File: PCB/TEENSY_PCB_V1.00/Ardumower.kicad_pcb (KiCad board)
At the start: 2 copper layers, 169.8 x 97 mm, 48 parts, among them J10 Sonar_R, J12 Sonar_L, J13 P_Right, J14 Buzzer, J15 Button, J19 P_Left, J2 I2C2, J21 PCB_2, J23 Ser1, J25 5V IN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

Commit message: gy521 test
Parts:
- added JP1: Jumper_3.3V, Connector_PinSocket_2.54mm:PinSocket_1x03_P2.54mm_Vertical, F.Cu at (256.7, 60.1)
- added U2: MAX5215, teensy_library-master:GY-521, F.Cu at (77.9, 29.0)
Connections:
- D8 pad 1: +3V3 -> Net-(D8-Pad1)
- U3 pad 46: (no net) -> Net-(JP1-Pad3)

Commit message: test
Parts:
- removed J21: PCB_2, Connector_JST:JST_XH_B6B-XH-A_1x06_P2.50mm_Vertical
- removed J23: Ser1, Connector_JST:JST_XH_B5B-XH-A_1x05_P2.50mm_Vertical
- removed J38: ODO_Left, Connector_JST:JST_XH_B4B-XH-A_1x04_P2.50mm_Vertical
- removed J39: ODO_Right, Connector_JST:JST_XH_B4B-XH-A_1x04_P2.50mm_Vertical
- removed J40: Motor_Right1, Connector_JST:JST_XH_B5B-XH-A_1x05_P2.50mm_Vertical
- removed J41: Motor_Left1, Connector_JST:JST_XH_B5B-XH-A_1x05_P2.50mm_Vertical
- removed J42: Cutter, Connector_JST:JST_XH_B5B-XH-A_1x05_P2.50mm_Vertical
- removed R14: 1KO, Resistor_THT:R_Axial_DIN0207_L6.3mm_D2.5mm_P2.54mm_Vertical
- removed R16, R17: 1,5KO, Resistor_THT:R_Axial_DIN0207_L6.3mm_D2.5mm_P2.54mm_Vertical
- added J1: ODO_Left, Connector_JST:JST_XH_B4B-XH-A_1x04_P2.50mm_Vertical, F.Cu at (168.5, 111.0)
- added J11: Cutter, Connector_JST:JST_XH_B5B-XH-A_1x05_P2.50mm_Vertical, F.Cu at (185.5, 95.4)
- added J16: Power_Board, Connector_JST:JST_XH_B6B-XH-A_1x06_P2.50mm_Vertical, F.Cu at (43.7, 102.6)
- added J6: ODO_Right, Connector_JST:JST_XH_B4B-XH-A_1x04_P2.50mm_Vertical, F.Cu at (185.5, 103.2)
- added J7: Motor_Right1, Connector_JST:JST_XH_B5B-XH-A_1x05_P2.50mm_Vertical, F.Cu at (168.5, 95.4)
- added J8: Motor_Left1, Connector_JST:JST_XH_B5B-XH-A_1x05_P2.50mm_Vertical, F.Cu at (168.5, 103.2)
- added JP3: MotorPower, Connector_PinSocket_2.54mm:PinSocket_1x03_P2.54mm_Vertical, F.Cu at (201.3, 94.3)
- added R12: 1,5KO, Resistor_THT:R_Axial_DIN0207_L6.3mm_D2.5mm_P2.54mm_Vertical, F.Cu at (193.8, 113.4)
- added R13: 1,5KO, Resistor_THT:R_Axial_DIN0207_L6.3mm_D2.5mm_P2.54mm_Vertical, F.Cu at (199.9, 113.4)
- added R5: 1KO, Resistor_THT:R_Axial_DIN0207_L6.3mm_D2.5mm_P2.54mm_Vertical, F.Cu at (181.5, 109.6)
- H1, H2, H3, H4: footprint MountingHole:MountingHole_2.2mm_M2_Pad_TopBottom -> MountingHole:MountingHole_3.2mm_M3_Pad_TopBottom
- J2: value I2C2 -> I2C2_0
- J3: value I2C0 -> I2C0_0
- J30: value I2C1 -> I2C1_0
- J4: value I2C3 -> I2C1_1
- JP4: value MotorPower -> Jumper; footprint Connector_PinSocket_2.54mm:PinSocket_1x03_P2.54mm_Vertical -> Connector_PinSocket_2.54mm:PinSocket_1x02_P2.54mm_Vertical
- R1, R3: value XXX -> XXXX
- U2: value MAX5215 -> GY-521
- moved JP1 214.8 mm to (43.2, 83.8), turned to 90 degrees
- moved J3 96.7 mm to (165.1, 85.1), turned to 0 degrees
- moved U2 87.3 mm to (67.3, 115.6), turned to 90 degrees
- moved JP5 68.6 mm to (198.8, 104.0), turned to 0 degrees
- moved U1 50.7 mm to (64.8, 72.4), turned to 90 degrees
- moved D2 39.8 mm to (43.2, 77.5)
- moved R6 39.4 mm to (187.7, 109.6), turned to 0 degrees
- moved R11 39.1 mm to (49.5, 77.5)
- moved U3 32.6 mm to (101.6, 99.1), turned to 180 degrees
- moved J10 17.8 mm to (170.1, 42.2)
- moved J12 17.8 mm to (179.9, 42.3)
- moved D7 14.9 mm to (52.4, 42.7)
- moved JP4 14.8 mm to (162.8, 71.9), turned to 0 degrees
- moved D8 13.6 mm to (52.4, 57.1)
- moved J25 12.7 mm to (44.9, 45.5)
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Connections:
- JP4 pad 1: +5V -> Net-(JP4-Pad1)
- JP4 pad 2: Net-(J40-Pad1) -> +3V3
- R11 pad 2: (no net) -> +3V3
- R3 pad 1: SDA0 -> +3V3
- R3 pad 2: +3V3 -> SDA0
- R6 pad 2: pinOdometryRight -> pinOdometryLeft
- U2 pad 1: (no net) -> +3V3
- U2 pad 2: (no net) -> GND
- U2 pad 7: +3V3 -> Net-(JP4-Pad1)
- U2 pad 8: GND -> (no net)
- U3 pad 32: pinChargeCurrent -> (no net)
- U3 pad 33: pinChargeVoltage -> (no net)
- U3 pad 43: pinBatteryVoltage -> (no net)
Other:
- board text added: "SCL2"
- board text added: "SDA2"
- board text added: "pinChargeEnable"
- board text removed: "+3.3V DUE"
- board text removed: "+3.3V IN"
- board text removed: "+5V DUE"
- board text removed: "+5V IN"
- board text removed: "+9V"
- board text removed: "C Power"
- board text removed: "DIR"
- board text removed: "EN"
- board text removed: "IOREV"
- board text removed: "M Power"
- board text removed: "MowFault"
- board text removed: "MowSense"
- board text removed: "PWM"
- board text removed: "Power"
- board text removed: "RX0"
- board text removed: "RX1"
- board text removed: "RX2"
- board text removed: "SCL0"
- board text removed: "SDA0"
- board text removed: "TX0"
- board text removed: "TX1"
- board text removed: "TX2"
- board text removed: "pinBatteryVoltage"
- board text removed: "pinChargeCurrent"
- board text removed: "pinChargeRelay"
- board text removed: "pinChargeVoltage"

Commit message: test
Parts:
- removed JP2: Buzzer OFF, Connector_PinSocket_2.54mm:PinSocket_1x02_P2.54mm_Vertical
- added BT1: Battery_Cell, Battery:BatteryHolder_Keystone_103_1x20mm, F.Cu at (136.0, 47.6)
- J1 ODO LEFT: renamed from J1
- J11 MOW MOTOR: renamed from J11
- J6 ODO RIGHT: renamed from J6
- J7 MOTOR RIGHT: renamed from J7
- J8 MOTOR LEFT: renamed from J8
- moved JP4 118.5 mm to (44.5, 67.3), turned to 90 degrees
- moved SP1 111.2 mm to (148.6, 68.6)
- moved J3 107.9 mm to (67.3, 39.5), turned to 270 degrees
- moved JP3 81.9 mm to (120.7, 80.0), turned to 90 degrees
- moved JP5 80.7 mm to (120.7, 83.8), turned to 90 degrees
- moved R12 79.2 mm to (118.1, 90.2)
- moved R13 78.0 mm to (124.5, 94.0)
- moved R10 70.3 mm to (69.2, 56.9)
- moved R7 70.3 mm to (79.1, 57.0)
- moved R8 70.3 mm to (74.4, 56.9)
- moved R9 70.3 mm to (64.4, 57.0)
- moved J14 69.4 mm to (158.8, 99.1), turned to 270 degrees
- moved J5 67.4 mm to (122.6, 58.5)
- moved J9 67.4 mm to (136.4, 58.4)
- moved J19 67.3 mm to (105.2, 58.5)
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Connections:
- J10 pad 3: (no net) -> pinSonarRightTrigger
- J10 pad 4: (no net) -> pinSonarRightEcho
- J12 pad 3: (no net) -> pinSonarLeftTrigger
- J12 pad 4: (no net) -> pinSonarLeftEcho
- SP1 pad 2: Net-(JP2-Pad2) -> pinBuzzer
- U3 pad 18: (no net) -> pinSonarLeftEcho
- U3 pad 19: (no net) -> pinSonarRightEcho
- U3 pad 20: (no net) -> pinSonarLeftTrigger
- U3 pad 21: (no net) -> pinSonarRightTrigger
- U3 pad 50: (no net) -> Net-(BT1-Pad1)
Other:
- board size 169.8 x 97 mm -> 141.9 x 100 mm
- board text added: "DIR"
- board text added: "EN"
- board text added: "PWM"
- board text added: "SCL0"
- board text added: "SDA0"
- board text added: "SIG"
- board text removed: "OUT"

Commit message: teensy pcb
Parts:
- removed JP4: Jumper, Connector_PinSocket_2.54mm:PinSocket_1x02_P2.54mm_Vertical
- removed U1: DOIT-ESP32-DEVKIT-V1, teensy_library-master:ESP32-DOIT-DEVKIT
- added J17: Power_PCB2, Connector_JST:JST_XH_B2B-XH-A_1x02_P2.50mm_Vertical, F.Cu at (43.7, 101.6)
- added J18 FRE 01 02: Free01_02, Connector_JST:JST_XH_B3B-XH-A_1x03_P2.50mm_Vertical, F.Cu at (173.6, 112.0)
- added J20 CAN3: Can3, Connector_JST:JST_XH_B5B-XH-A_1x05_P2.50mm_Vertical, F.Cu at (97.8, 123.2)
- added J21 SER5: Ser5, Connector_JST:JST_XH_B5B-XH-A_1x05_P2.50mm_Vertical, F.Cu at (154.7, 104.1)
- added J22 FREE A16 A17: FreeA16_A17, Connector_JST:JST_XH_B4B-XH-A_1x04_P2.50mm_Vertical, F.Cu at (173.2, 102.4)
- added J23 ES32 RFID1: ESP RFID1, Connector_JST:JST_XH_B5B-XH-A_1x05_P2.50mm_Vertical, F.Cu at (120.1, 123.4)
- added J24 ESP32 RFID2: ESP RFID2, Connector_JST:JST_XH_B5B-XH-A_1x05_P2.50mm_Vertical, F.Cu at (138.1, 123.2)
- added J26 ESP32 IC2: ESP32 I2C, Connector_JST:JST_XH_B4B-XH-A_1x04_P2.50mm_Vertical, F.Cu at (158.2, 126.7)
- added R14: XXX, Resistor_THT:R_Axial_DIN0207_L6.3mm_D2.5mm_P2.54mm_Vertical, F.Cu at (159.8, 120.1)
- added R15: XXX, Resistor_THT:R_Axial_DIN0207_L6.3mm_D2.5mm_P2.54mm_Vertical, F.Cu at (166.0, 120.1)
- added U4: ESP32-DEVKIT-V1, teensy_library-master:ESP32-DEVKIT-V1, F.Cu at (99.1, 90.9)
- J11: renamed from J11 MOW MOTOR
- J16: value Power_Board -> Power_PCB1
- J7: renamed from J7 MOTOR RIGHT
- J8: renamed from J8 MOTOR LEFT
- moved J31 34.6 mm to (136.6, 104.3)
- moved SP1 27.3 mm to (170.6, 52.5)
- moved R12 20.4 mm to (133.6, 77.0)
- moved R13 20.4 mm to (140.0, 80.8)
- moved R5 20.4 mm to (133.6, 80.8)
- moved R6 20.4 mm to (140.0, 77.0)
- moved J11 20.4 mm to (174.2, 66.8)
- moved J7 20.4 mm to (151.4, 66.8)
- moved J8 20.4 mm to (161.5, 66.8)
- moved JP3 20.4 mm to (136.1, 66.8)
- moved JP5 20.4 mm to (136.1, 70.6)
- moved J6 ODO RIGHT 11.3 mm to (128.8, 90.4), turned to 0 degrees
- moved D2 9.92 mm to (55.9, 128.3)
- moved J14 9.00 mm to (160.8, 90.3), turned to 0 degrees
- moved J1 ODO LEFT 8.87 mm to (144.7, 90.3), turned to 0 degrees
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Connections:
- J16 pad 1: pinChargeEnable -> SCL1
- J16 pad 2: pinBatterySwitch -> SDA1
- J16 pad 3: SCL2 -> SCL0
- J16 pad 4: SDA2 -> SDA0
- U2 pad 7: Net-(JP4-Pad1) -> (no net)
- U3 pad 22: (no net) -> CRX3
- U3 pad 23: (no net) -> CTX3
- U3 pad 24: (no net) -> Free02
- U3 pad 32: (no net) -> FreeA16
- U3 pad 33: (no net) -> FreeA17
- U3 pad 35: (no net) -> Free01
- U3 pad 42: (no net) -> TX5
- U3 pad 43: (no net) -> RX5
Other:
- board text added: "PinBatterySwitch"
- board text added: "PinChargeEnable"
- board text added: "RX5"
- board text added: "TX5"
- board text removed: "pinBatterySwitch"
- board text removed: "pinChargeEnable"

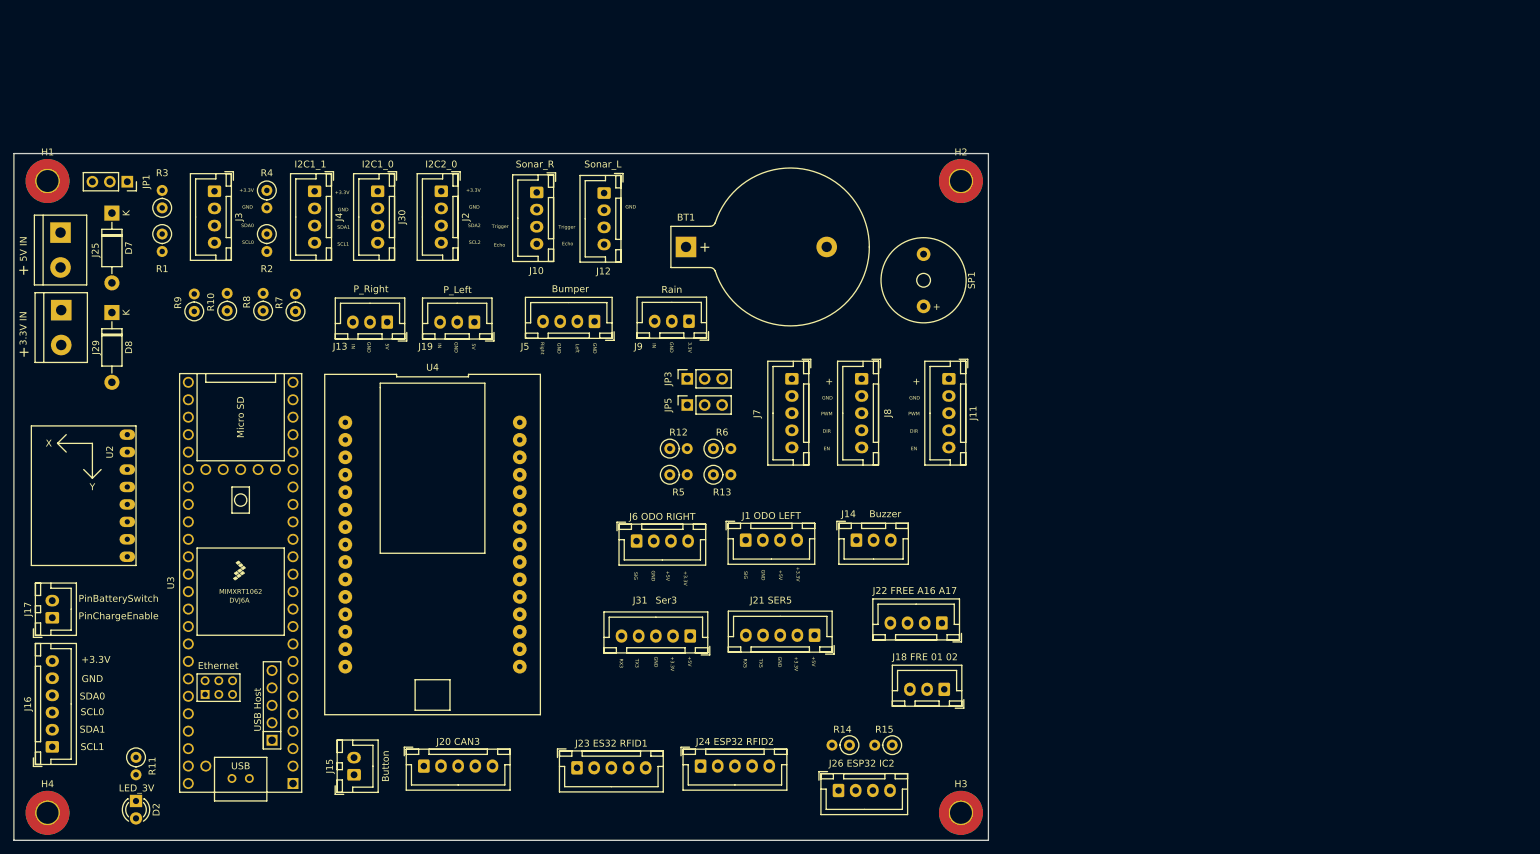
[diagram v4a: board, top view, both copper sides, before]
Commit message: ordered teensy pcb
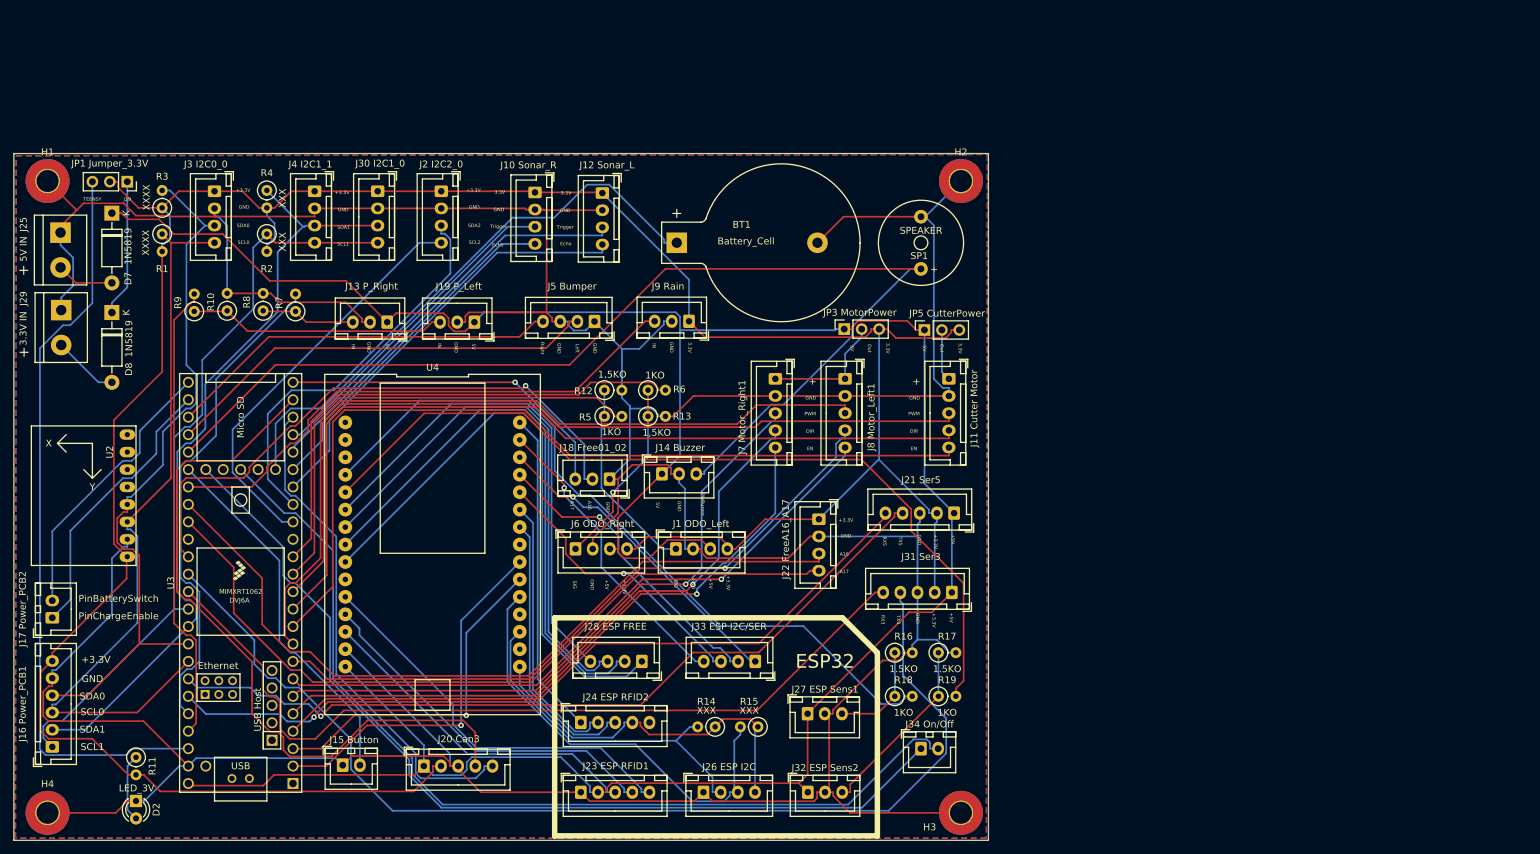
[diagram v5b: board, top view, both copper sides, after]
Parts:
- added J27 ESP Sens1: ESP32 Sens1, Connector_JST:JST_XH_B3B-XH-A_1x03_P2.50mm_Vertical, F.Cu at (153.7, 115.6)
- added J28 ESP FREE: ESP32 FREE, Connector_JST:JST_XH_B4B-XH-A_1x04_P2.50mm_Vertical, F.Cu at (129.5, 108.0)
- added J32 ESP Sens2: ESP32 Sens2, Connector_JST:JST_XH_B3B-XH-A_1x03_P2.50mm_Vertical, F.Cu at (153.7, 127.0)
- added J33 ESP I2C/SER: ESP32 I2C/SER, Connector_JST:JST_XH_B4B-XH-A_1x04_P2.50mm_Vertical, F.Cu at (146.1, 108.0)
- added J34 On/Off: Teensy On/Off, Connector_JST:JST_XH_B2B-XH-A_1x02_P2.50mm_Vertical, F.Cu at (170.2, 120.7)
- added R16: 1.5KO, Resistor_THT:R_Axial_DIN0207_L6.3mm_D2.5mm_P2.54mm_Vertical, F.Cu at (166.4, 106.7)
- added R17: 1.5KO, Resistor_THT:R_Axial_DIN0207_L6.3mm_D2.5mm_P2.54mm_Vertical, F.Cu at (172.7, 106.7)
- added R18: 1KO, Resistor_THT:R_Axial_DIN0207_L6.3mm_D2.5mm_P2.54mm_Vertical, F.Cu at (166.4, 113.0)
- added R19: 1KO, Resistor_THT:R_Axial_DIN0207_L6.3mm_D2.5mm_P2.54mm_Vertical, F.Cu at (172.7, 113.0)
- J1 ODO_Left: renamed from J1 ODO LEFT
- J10 Sonar_R: renamed from J10
- J11 Cutter Motor: renamed from J11
- J12 Sonar_L: renamed from J12
- J13 P_Right: renamed from J13
- J14 Buzzer: renamed from J14
- J15 Button: renamed from J15
- J16 Power_PCB1: renamed from J16
- J17 Power_PCB2: renamed from J17
- J18 Free01_02: renamed from J18 FRE 01 02
- J19 P_Left: renamed from J19
- J2 I2C2_0: renamed from J2
- J20 Can3: renamed from J20 CAN3
- J21 Ser5: renamed from J21 SER5
- J22 FreeA16_A17: renamed from J22 FREE A16 A17
- J23 ESP RFID1: renamed from J23 ES32 RFID1
- J24 ESP RFID2: renamed from J24 ESP32 RFID2
- J26 ESP I2C: renamed from J26 ESP32 IC2
- J3 I2C0_0: renamed from J3
- J30 I2C1_0: renamed from J30
- J31 Ser3: renamed from J31
- J4 I2C1_1: renamed from J4
- J5 Bumper: renamed from J5
- J6 ODO_Right: renamed from J6 ODO RIGHT
- J7 Motor_Right1: renamed from J7
- J8 Motor_Left1: renamed from J8
- J9 Rain: renamed from J9
- JP1 Jumper_3.3V: renamed from JP1
- JP3 MotorPower: renamed from JP3
- JP5 CutterPower: renamed from JP5
- moved J18 Free01_02 57.5 mm to (124.8, 81.4)
- moved J31 Ser3 38.6 mm to (174.7, 97.9)
- moved JP5 CutterPower 36.2 mm to (170.7, 59.7)
- moved J14 Buzzer 29.9 mm to (132.5, 80.6)
- moved J21 Ser5 27.0 mm to (175.0, 86.4)
- moved JP3 MotorPower 24.0 mm to (159.0, 59.6)
- moved J22 FreeA16_A17 23.4 mm to (155.3, 87.2), turned to 270 degrees
- moved R14 19.7 mm to (140.2, 117.5)
- moved R15 19.7 mm to (146.4, 117.5)
- moved J26 ESP I2C 19.7 mm to (138.5, 127.0)
- moved J24 ESP RFID2 18.6 mm to (120.7, 116.8)
- moved R12 12.8 mm to (124.1, 68.5)
- moved R5 12.8 mm to (124.1, 72.3)
- moved R13 12.8 mm to (130.4, 72.3)
- moved R6 12.8 mm to (130.4, 68.5)
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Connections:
- U3 pad 52: (no net) -> Net-(J34-Pad2)
- U3 pad 54: (no net) -> Net-(J34-Pad1)
- U4 pad 26: (no net) -> Net-(J33-Pad3)
- U4 pad 27: (no net) -> Net-(J33-Pad2)
- U4 pad 28: (no net) -> Net-(J33-Pad1)
- U4 pad 29: (no net) -> Net-(J33-Pad4)
- U4 pad 4: (no net) -> Net-(R18-Pad2)
- U4 pad 5: (no net) -> Net-(R19-Pad2)
- U4 pad 6: (no net) -> Net-(J28-Pad4)
- U4 pad 7: (no net) -> Net-(J28-Pad3)
- U4 pad 8: (no net) -> Net-(J28-Pad2)
- U4 pad 9: (no net) -> Net-(J28-Pad1)
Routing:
- net GND: track 0.00 -> 665.7 mm
- net +3V3: track 0.00 -> 387.7 mm
- net +5V: track 0.00 -> 380.7 mm
- net pinBuzzer: track 0.00 -> 163.8 mm
- net TX3: track 0.00 -> 158.9 mm
- net Net-(J34-Pad2): track 0.00 -> 139.1 mm
- net Net-(J34-Pad1): track 0.00 -> 137.2 mm
- net pinMotorMowEnable: track 0.00 -> 126.5 mm
- net Net-(R19-Pad2): track 0.00 -> 123.8 mm
- net pinMotorMowDir: track 0.00 -> 123.7 mm
- net RX3: track 0.00 -> 123.2 mm
- net pinMotorMowPWM: track 0.00 -> 121.6 mm
- net TX5: track 0.00 -> 118.8 mm, vias 0 -> 1
- net pinMotorLeftPWM: track 0.00 -> 116.8 mm
- net RX5: track 0.00 -> 116.0 mm, vias 0 -> 1
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- added copper zone on B.Cu, net GND
- added copper zone on F.Cu, net GND
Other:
- rule trace_min: 0.254 -> 0.25
- board text added: "A16"
- board text added: "A17"
- board text added: "ESP32"
- board text added: "J29"
- board text added: "Out"
- board text added: "PinBuzzer"
- board text added: "TEENSY"
